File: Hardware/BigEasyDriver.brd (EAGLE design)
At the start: 36.8 x 30.5 mm, 53 parts, among them IC1 A4983ALT1, IC2 LM317L

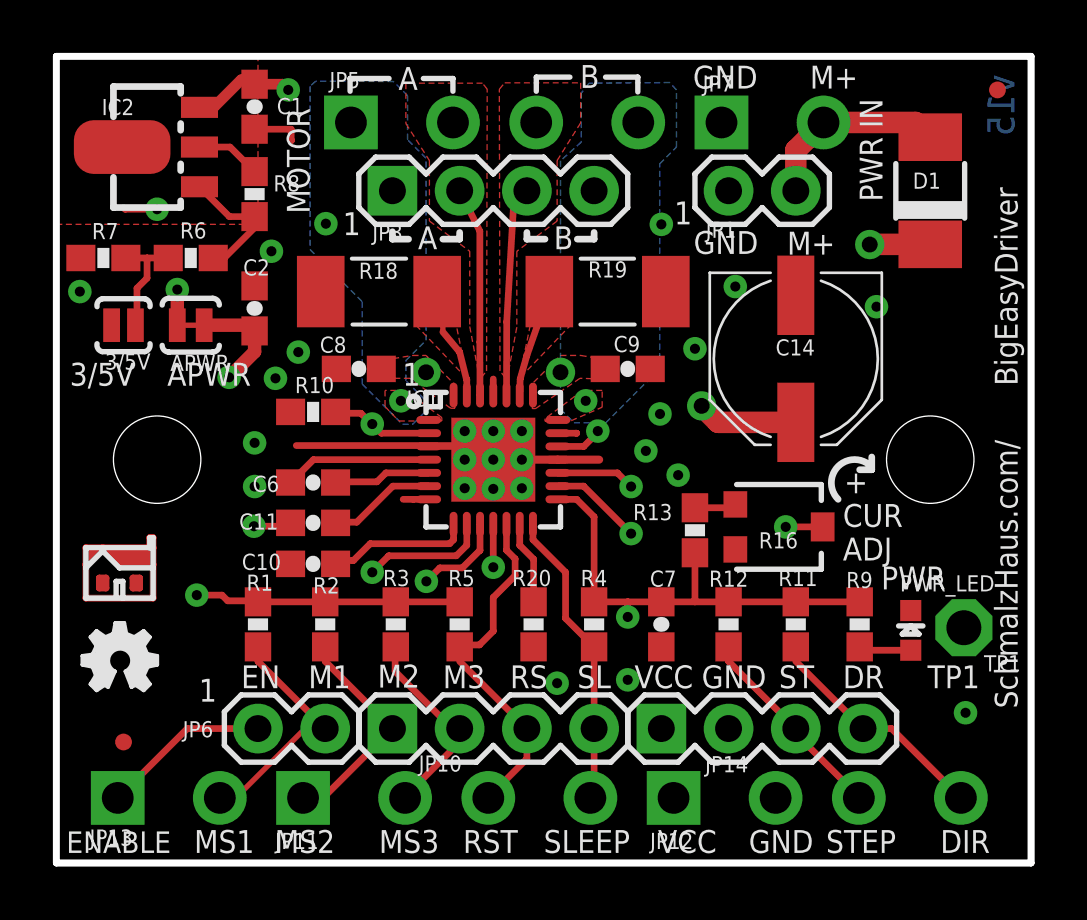
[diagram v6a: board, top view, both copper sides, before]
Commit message: Frame updated, Angles , Creative Commons added
Added new schematic framrs, cleaned up some trace angels and added the
creative commons license.
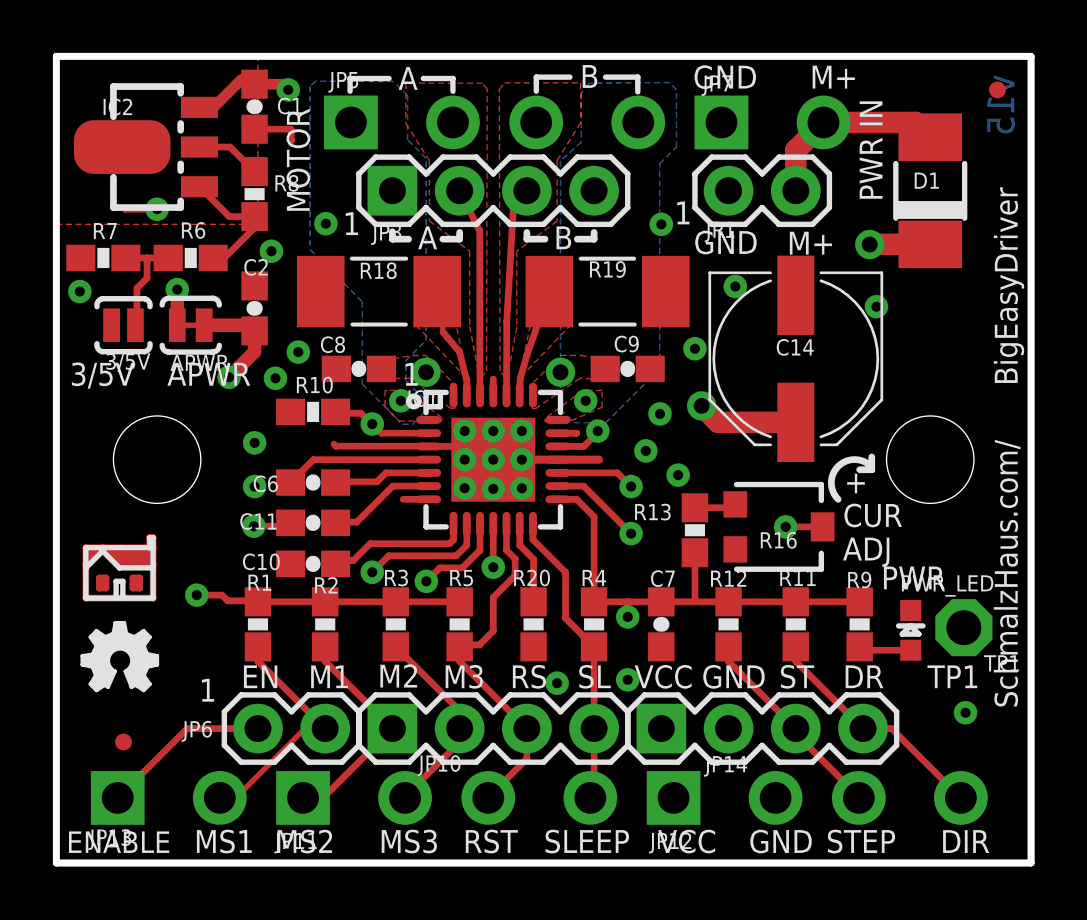
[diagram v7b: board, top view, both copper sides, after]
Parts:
- added FRAME1: FRAME-LETTER, SparkFun-Aesthetics:CREATIVE_COMMONS
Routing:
- net GND: track 12.8 -> 11.0 mm
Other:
- board text added: "Brian Schmalz"
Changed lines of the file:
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@@
 <layer number="19" name="Unrouted" color="11" fill="1" visible="yes" active="yes"/>
 <layer number="20" name="Dimension" color="6" fill="1" visible="yes" active="yes"/>
-<layer number="21" name="tPlace" color="16" fill="1" visible="yes" active="yes"/>
-<layer number="22" name="bPlace" color="14" fill="1" visible="yes" active="yes"/>
+<layer number="21" name="tPlace" color="16" fill="1" visible="no" active="yes"/>
+<layer number="22" name="bPlace" color="14" fill="1" visible="no" active="yes"/>
 <layer number="23" name="tOrigins" color="15" fill="1" visible="yes" active="yes"/>
 <layer number="24" name="bOrigins" color="15" fill="1" visible="yes" active="yes"/>
@@
 <layer number="144" name="DrillLegend" color="7" fill="1" visible="no" active="yes"/>
 <layer number="151" name="HeatSink" color="7" fill="1" visible="no" active="no"/>
+<layer number="199" name="Contour" color="7" fill="1" visible="no" active="yes"/>
 <layer number="200" name="200bmp" color="1" fill="10" visible="no" active="no"/>
 <layer number="201" name="201bmp" color="2" fill="1" visible="no" active="no"/>
@@
 <wire x1="30.353" y1="14.859" x2="30.8102" y2="14.859" width="0.254" layer="21"/>
 <wire x1="30.8102" y1="14.859" x2="30.8102" y2="15.3416" width="0.254" layer="21"/>
+<text x="-57.15" y="0" size="1.778" layer="27" font="vector">Brian Schmalz</text>
 </plain>
 <attributes>
@@
 <param name="dpGapFactor" value="2.5"/>
 <param name="checkGrid" value="0"/>
-<param name="checkAngle" value="0"/>
+<param name="checkAngle" value="1"/>
 <param name="checkFont" value="1"/>
 <param name="checkRestrict" value="1"/>
@@
 <element name="U$4" library="Testing" package="PAD-0.008" value="PAD" x="19.6596" y="16.2306"/>
 <element name="U$5" library="Testing" package="PAD-0.008" value="PAD" x="16.51" y="18.288"/>
+<element name="FRAME1" library="SparkFun-Aesthetics" package="CREATIVE_COMMONS" value="FRAME-LETTER" x="-87.98265625" y="0"/>
 </elements>
 <signals>
@@
 <contactref element="JP12" pad="2"/>
 <contactref element="C2" pad="2"/>
-<wire x1="15.2955" y1="15.74" x2="14.0701" y2="15.74" width="0.254" layer="1"/>
 <wire x1="15.3035" y1="15.748" x2="15.2955" y2="15.74" width="0.254" layer="1"/>
 <wire x1="17.5895" y1="15.24" x2="18.9499" y2="15.24" width="0.3048" layer="1"/>
@@
 </polygon>
 <wire x1="15.3035" y1="15.748" x2="15.3035" y2="15.7734" width="0.254" layer="1"/>
-<wire x1="15.3035" y1="15.7734" x2="9.0678" y2="15.7734" width="0.254" layer="1"/>
 <wire x1="7.493" y1="27.725" x2="8.875" y2="27.725" width="0.254" layer="1"/>
 <wire x1="8.875" y1="27.725" x2="8.875" y2="27.29" width="0.254" layer="1"/>
+<wire x1="14.0701" y1="15.74" x2="15.4305" y2="15.74" width="0.254" layer="1"/>
+<wire x1="15.4305" y1="15.74" x2="15.4305" y2="15.24" width="0.254" layer="1"/>
+<wire x1="10.4902" y1="15.8242" x2="10.5664" y2="15.748" width="0.254" layer="1"/>
+<wire x1="10.5664" y1="15.748" x2="14.224" y2="15.748" width="0.254" layer="1"/>
 </signal>
 <signal name="VCC">
@@
 <contactref element="JP12" pad="1"/>
 <contactref element="R13" pad="1"/>
-<wire x1="7.62" y1="20.32" x2="7.493" y2="20.105" width="0.508" layer="1"/>
 <wire x1="25.4" y1="9.867" x2="27.94" y2="9.867" width="0.254" layer="1"/>
 <wire x1="7.62" y1="9.867" x2="10.16" y2="9.867" width="0.254" layer="1"/>
@@
 <contactref element="JP12" pad="4"/>
 <wire x1="19.931" y1="15.74" x2="18.95" y2="15.74" width="0.254" layer="1"/>
-<wire x1="30.48" y1="5.08" x2="30.48" y2="5.7" width="0.254" layer="1"/>
 <wire x1="31.5578" y1="5.08" x2="30.48" y2="5.08" width="0.254" layer="1"/>
 <wire x1="34.1778" y1="2.46" x2="31.5578" y2="5.08" width="0.254" layer="1"/>
@@
 <wire x1="20.4597" y1="16.3195" x2="20.4597" y2="16.2687" width="0.254" layer="1"/>
 <via x="20.4597" y="16.3195" extent="1-16" drill="0.381"/>
-<wire x1="30.48" y1="5.7" x2="29.86" y2="5.7" width="0.254" layer="1"/>
-<wire x1="29.86" y1="5.7" x2="27.94" y2="7.62" width="0.254" layer="1"/>
-<wire x1="27.94" y1="7.62" x2="27.94" y2="8.167" width="0" layer="19" extent="1-1"/>
+<wire x1="30.48" y1="5.08" x2="27.94" y2="7.62" width="0.254" layer="1"/>
+<wire x1="27.94" y1="7.62" x2="27.94" y2="8.167" width="0.254" layer="1"/>
 </signal>
 <signal name="MS1">
@@
 <wire x1="16.3222" y1="2.46" x2="16.3222" y2="2.4792" width="0.254" layer="1"/>
 <wire x1="16.3222" y1="2.4792" x2="17.78" y2="3.937" width="0.254" layer="1"/>
-<wire x1="17.78" y1="3.937" x2="17.78" y2="5.08" width="0.254" layer="1"/>
 <wire x1="17.01" y1="11.819" x2="17.01" y2="12.8" width="0.254" layer="1"/>
 <wire x1="17.3355" y1="11.4935" x2="17.01" y2="11.819" width="0.254" layer="1"/>
@@
 <wire x1="16.51" y1="8.763" x2="16.51" y2="10.033" width="0.254" layer="1"/>
 <wire x1="15.987" y1="8.24" x2="16.51" y2="8.763" width="0.254" layer="1"/>
-<wire x1="17.78" y1="5.08" x2="17.78" y2="5.7" width="0.254" layer="1"/>
 <wire x1="15.987" y1="8.24" x2="15.313" y2="8.24" width="0.254" layer="1"/>
 <wire x1="15.313" y1="8.24" x2="15.24" y2="8.167" width="0.254" layer="1"/>
-<wire x1="17.78" y1="5.7" x2="17.16" y2="5.7" width="0.254" layer="1"/>
-<wire x1="17.16" y1="5.7" x2="15.24" y2="7.62" width="0.254" layer="1"/>
-<wire x1="15.24" y1="7.62" x2="15.24" y2="8.167" width="0" layer="19" extent="1-1"/>
+<wire x1="17.78" y1="5.08" x2="15.24" y2="7.62" width="0.254" layer="1"/>
+<wire x1="15.24" y1="7.62" x2="15.24" y2="8.167" width="0.254" layer="1"/>
+<wire x1="17.78" y1="3.937" x2="17.78" y2="5.08" width="0.254" layer="1"/>
 </signal>
 <signal name="STEP">
@@
 <contactref element="IC2" pad="OUT@1"/>
 <contactref element="APWR" pad="1"/>
-<wire x1="7.224" y1="26.05" x2="7.493" y2="26.123" width="0.254" layer="1"/>
 <wire x1="4.572" y1="20.32" x2="4.572" y2="21.6662" width="0.508" layer="1"/>
 <wire x1="4.572" y1="21.6662" x2="4.572" y2="23.9395" width="0.508" layer="2"/>
@@
 <wire x1="15.24" y1="5.08" x2="16.51" y2="6.35" width="0.254" layer="2"/>
 <via x="16.51" y="11.176" extent="1-16" drill="0.381"/>
-<wire x1="15.24" y1="5.08" x2="14.9606" y2="5.08" width="0.254" layer="1"/>
-<wire x1="14.9606" y1="5.08" x2="12.8016" y2="7.239" width="0.254" layer="1"/>
-<wire x1="12.8016" y1="7.239" x2="12.8016" y2="8.1416" width="0.254" layer="1"/>
-<wire x1="12.8016" y1="8.1416" x2="12.827" y2="8.167" width="0.254" layer="1"/>
+<wire x1="12.827" y1="8.167" x2="15.24" y2="5.754" width="0.254" layer="1"/>
+<wire x1="15.24" y1="5.754" x2="15.24" y2="5.08" width="0.254" layer="1"/>
 </signal>
 <signal name="N$1">
@@
 <contactref element="IC1" pad="P$7"/>
 <contactref element="U$3" pad="P$1"/>
-<wire x1="14.0701" y1="13.74" x2="13.4888" y2="13.74" width="0.254" layer="1"/>
-<wire x1="13.4888" y1="13.74" x2="13.1064" y2="13.7414" width="0.254" layer="1"/>
+<wire x1="14.0701" y1="13.74" x2="14.0701" y2="13.7414" width="0.254" layer="1"/>
+<wire x1="14.0701" y1="13.7414" x2="13.1064" y2="13.7414" width="0.254" layer="1"/>
 </signal>
 <signal name="N$7">

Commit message: Version 1.6 update -
* Removed large hole on bottom solder mask (because vias will short out with plane if a metal heatsink is used, this is kinda pointless)
* Changed R13 to 8.3K to give much more useful range of pot motion
* Added current limiting resistors to STEP and DIR lines
* got rid of all angle errors in DRC
* Added more explanation of R16 current adjust pot behavior in schematic
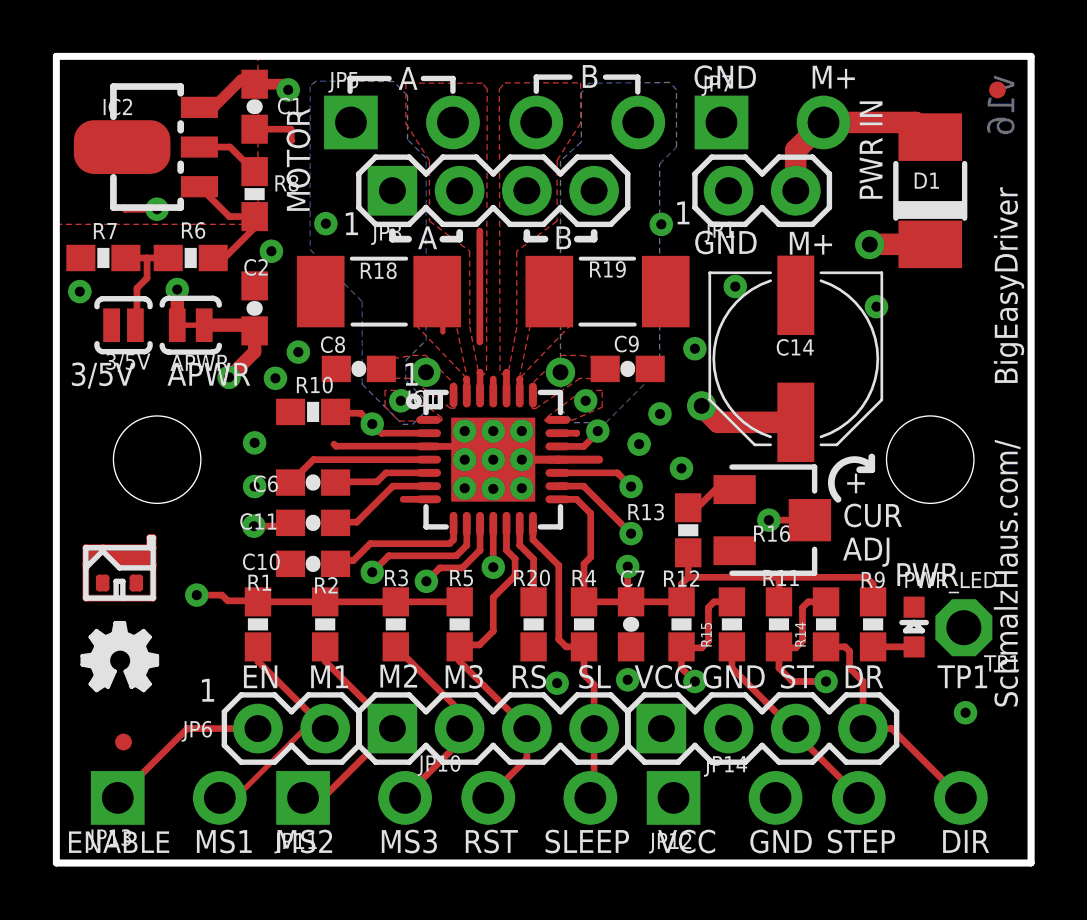
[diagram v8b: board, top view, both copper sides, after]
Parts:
- added R14, R15: 1K, SparkFun:0603-RES
- R13: value 2.49K -> 8.2K
- R16: device SparkFun:TRIMPOT-3MM -> SparkFun-Electromechanical:TRIMPOT-3MM-2
- moved R12 1.78 mm to (23.6, 9.02)
- moved C7 1.14 mm to (21.7, 9.02)
- moved R11 0.64 mm to (27.3, 9.02)
- moved R9 0.51 mm to (30.9, 9.02)
- moved R4 0.38 mm to (19.9, 9.02)
- moved R16 0.36 mm to (27.1, 13.0)
- moved R13 0.25 mm to (23.9, 12.6)
- moved PWR_LED 0.18 mm to (32.4, 8.92)
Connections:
- new net N$55: JP12.4, JP14.4, R14.1
- new net N$56: JP12.3, JP14.3, R15.1
- net DIR: now also R14.2; no longer JP12.4, JP14.4
- net STEP: now also R15.2; no longer JP12.3, JP14.3
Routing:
- net N$55: track 0.00 -> 8.87 mm
- net N$56: track 0.00 -> 7.77 mm
- net COILA-: track 7.95 -> 0.87 mm
- net STEP: track 21.2 -> 15.0 mm, vias 1 -> 2
- net DIR: track 26.7 -> 21.7 mm, vias 1 -> 2
- net N$32: track 4.09 -> 0.61 mm
- net VCC: track 31.5 -> 34.8 mm
- net COILB-: track 7.94 -> 5.06 mm
- net N$31: track 4.30 -> 2.27 mm
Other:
- board text added: "Brian Schmalz: http://schmalzhaus.com/BigEasyDriver/index.html"
- board text added: "v16"
- board text removed: "Brian Schmalz"
- board text removed: "v15"
